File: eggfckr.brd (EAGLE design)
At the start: 91.1 x 31.7 mm, 7 parts, among them U1 ATTINY85-20PU

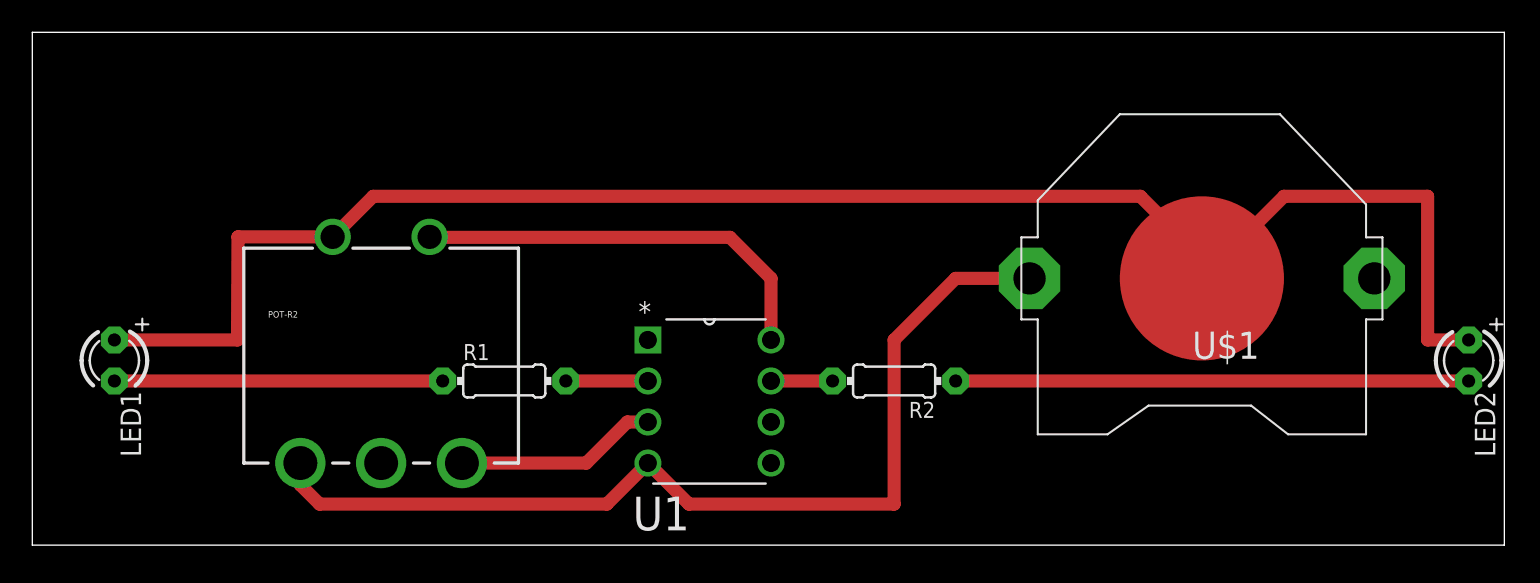
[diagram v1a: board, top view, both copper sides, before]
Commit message: failed linear to log pot convertion
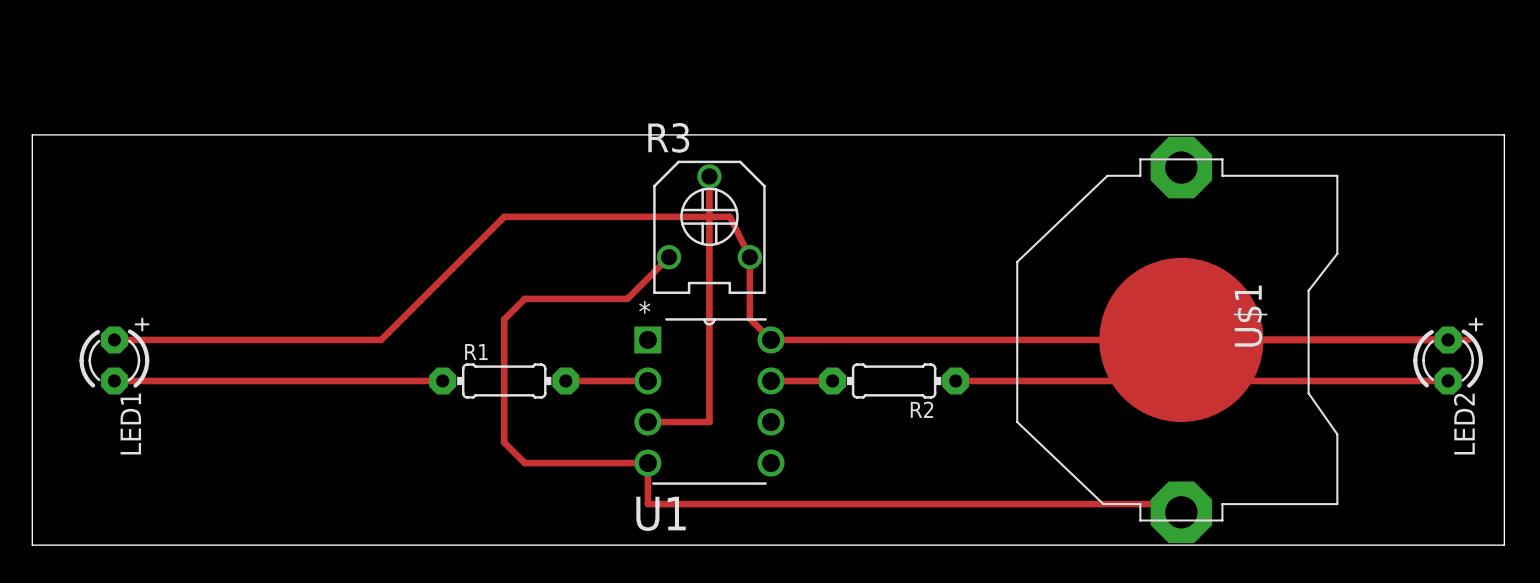
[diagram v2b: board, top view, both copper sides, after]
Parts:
- removed POT-R2: 5K, SparkFun-Electromechanical:POT_PTH
- added R3: (no value), dp_devices:TRIMMER_3306F
- moved U$1 4.02 mm to (71.1, 12.7), turned to 270 degrees
- moved LED2 1.27 mm to (87.6, 11.4)
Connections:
- removed net N$3: POT-R2.S2, U1.8
- net GND: now also R3.1; no longer POT-R2.E@1
- net N$2: now also R3.2; no longer POT-R2.E@2
- net VCC: now also R3.3, U1.8; no longer POT-R2.S1
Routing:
- net N$3: track 26.0 -> 0.00 mm
- net N$2: track 12.6 -> 19.0 mm
- net GND: track 60.8 -> 64.6 mm
- net VCC: track 108.1 -> 109.4 mm
- net N$7: track 31.8 -> 30.5 mm
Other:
- board size 91.1 x 31.7 mm -> 91.1 x 25.4 mm
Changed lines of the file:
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@@
 <plain>
 <wire x1="0" y1="0" x2="91.11" y2="0" width="0" layer="20"/>
-<wire x1="91.11" y1="0" x2="91.11" y2="31.74" width="0" layer="20"/>
-<wire x1="91.11" y1="31.74" x2="0" y2="31.74" width="0" layer="20"/>
-<wire x1="0" y1="31.74" x2="0" y2="0" width="0" layer="20"/>
+<wire x1="91.11" y1="0" x2="91.11" y2="25.39" width="0" layer="20"/>
+<wire x1="91.11" y1="25.39" x2="0" y2="25.39" width="0" layer="20"/>
+<wire x1="0" y1="25.39" x2="0" y2="0" width="0" layer="20"/>
 </plain>
 <attributes>
@@
 </autorouter>
 <elements>
-<element name="POT-R2" library="SparkFun-Electromechanical" package="POT_PTH" value="5K" x="21.59" y="5.08"/>
 <element name="LED1" library="adafruit" package="LED3MM" value="" x="5.08" y="11.43" rot="R270"/>
 <element name="R2" library="adafruit" package="0204/7" value="" x="53.34" y="10.16" rot="R180"/>
@@
 </element>
 <element name="R1" library="adafruit" package="0204/7" value="" x="29.21" y="10.16"/>
-<element name="LED2" library="adafruit" package="LED3MM" value="" x="88.9" y="11.43" rot="R270"/>
-<element name="U$1" library="adafruit" package="CR2032-THRU" value="" x="72.39" y="16.51" rot="R180"/>
+<element name="LED2" library="adafruit" package="LED3MM" value="" x="87.63" y="11.43" rot="R270"/>
+<element name="U$1" library="adafruit" package="CR2032-THRU" value="" x="71.12" y="12.7" rot="R270"/>
+<element name="R3" library="dp_devices" package="TRIMMER_3306F" value="" x="41.91" y="20.32"/>
 </elements>
 <signals>
@@
 <contactref element="U1" pad="7"/>
 <contactref element="R2" pad="2"/>
-<wire x1="45.72" y1="10.16" x2="49.53" y2="10.16" width="0.8128" layer="1"/>
+<wire x1="49.53" y1="10.16" x2="45.72" y2="10.16" width="0.4064" layer="1"/>
 </signal>
 <signal name="N$6">
 <contactref element="R1" pad="1"/>
 <contactref element="LED1" pad="K"/>
-<wire x1="5.08" y1="10.16" x2="25.4" y2="10.16" width="0.8128" layer="1"/>
+<wire x1="25.4" y1="10.16" x2="5.08" y2="10.16" width="0.4064" layer="1"/>
 </signal>
 <signal name="N$7">
 <contactref element="R2" pad="1"/>
 <contactref element="LED2" pad="K"/>
-<wire x1="57.15" y1="10.16" x2="88.9" y2="10.16" width="0.8128" layer="1"/>
+<wire x1="87.63" y1="10.16" x2="57.15" y2="10.16" width="0.4064" layer="1"/>
 </signal>
 <signal name="GND">
 <contactref element="U1" pad="4"/>
-<contactref element="POT-R2" pad="E@1"/>
 <contactref element="U$1" pad="+2"/>
-<wire x1="16.59" y1="5.08" x2="16.59" y2="3.73" width="0.8128" layer="1"/>
-<wire x1="16.59" y1="3.73" x2="17.78" y2="2.54" width="0.8128" layer="1"/>
-<wire x1="17.78" y1="2.54" x2="35.56" y2="2.54" width="0.8128" layer="1"/>
-<wire x1="35.56" y1="2.54" x2="38.1" y2="5.08" width="0.8128" layer="1"/>
-<wire x1="61.722" y1="16.51" x2="57.15" y2="16.51" width="0.8128" layer="1"/>
-<wire x1="57.15" y1="16.51" x2="53.34" y2="12.7" width="0.8128" layer="1"/>
-<wire x1="53.34" y1="12.7" x2="53.34" y2="2.54" width="0.8128" layer="1"/>
-<wire x1="53.34" y1="2.54" x2="40.64" y2="2.54" width="0.8128" layer="1"/>
-<wire x1="40.64" y1="2.54" x2="38.1" y2="5.08" width="0.8128" layer="1"/>
+<contactref element="R3" pad="1"/>
+<wire x1="38.1" y1="5.08" x2="38.1" y2="2.54" width="0.4064" layer="1"/>
+<wire x1="38.1" y1="2.54" x2="70.612" y2="2.54" width="0.4064" layer="1"/>
+<wire x1="70.612" y1="2.54" x2="71.12" y2="2.032" width="0.4064" layer="1"/>
+<wire x1="38.1" y1="5.08" x2="30.48" y2="5.08" width="0.4064" layer="1"/>
+<wire x1="30.48" y1="5.08" x2="29.21" y2="6.35" width="0.4064" layer="1"/>
+<wire x1="29.21" y1="6.35" x2="29.21" y2="13.97" width="0.4064" layer="1"/>
+<wire x1="29.21" y1="13.97" x2="30.48" y2="15.24" width="0.4064" layer="1"/>
+<wire x1="30.48" y1="15.24" x2="36.83" y2="15.24" width="0.4064" layer="1"/>
+<wire x1="36.83" y1="15.24" x2="39.41" y2="17.82" width="0.4064" layer="1"/>
 </signal>
 <signal name="VCC">
-<contactref element="POT-R2" pad="S1"/>
 <contactref element="LED2" pad="A"/>
 <contactref element="LED1" pad="A"/>
 <contactref element="U$1" pad="-"/>
-<wire x1="88.9" y1="12.7" x2="86.36" y2="12.7" width="0.8128" layer="1"/>
-<wire x1="86.36" y1="12.7" x2="86.36" y2="21.59" width="0.8128" layer="1"/>
-<wire x1="86.36" y1="21.59" x2="77.47" y2="21.59" width="0.8128" layer="1"/>
-<wire x1="77.47" y1="21.59" x2="72.39" y2="16.51" width="0.8128" layer="1"/>
-<wire x1="72.39" y1="16.51" x2="71.12" y2="15.24" width="0.8128" layer="1"/>
-<wire x1="71.12" y1="15.24" x2="71.12" y2="16.51" width="0.8128" layer="1"/>
-<wire x1="72.39" y1="16.51" x2="72.39" y2="17.78" width="0.8128" layer="1"/>
-<wire x1="72.39" y1="17.78" x2="68.58" y2="21.59" width="0.8128" layer="1"/>
-<wire x1="68.58" y1="21.59" x2="21.1" y2="21.59" width="0.8128" layer="1"/>
-<wire x1="21.1" y1="21.59" x2="18.59" y2="19.08" width="0.8128" layer="1"/>
-<wire x1="18.59" y1="19.08" x2="12.73" y2="19.08" width="0.8128" layer="1"/>
-<wire x1="12.73" y1="19.08" x2="12.7" y2="12.7" width="0.8128" layer="1"/>
-<wire x1="12.7" y1="12.7" x2="5.08" y2="12.7" width="0.8128" layer="1"/>
-</signal>
-<signal name="N$3">
 <contactref element="U1" pad="8"/>
-<contactref element="POT-R2" pad="S2"/>
-<wire x1="45.72" y1="12.7" x2="45.72" y2="16.51" width="0.8128" layer="1"/>
-<wire x1="45.72" y1="16.51" x2="43.18" y2="19.05" width="0.8128" layer="1"/>
-<wire x1="43.18" y1="19.05" x2="24.62" y2="19.05" width="0.8128" layer="1"/>
-<wire x1="24.62" y1="19.05" x2="24.59" y2="19.08" width="0.8128" layer="1"/>
-</signal>
-<signal name="N$2">
-<contactref element="U1" pad="3"/>
-<contactref element="POT-R2" pad="E@2"/>
-<wire x1="26.59" y1="5.08" x2="34.29" y2="5.08" width="0.8128" layer="1"/>
-<wire x1="34.29" y1="5.08" x2="36.83" y2="7.62" width="0.8128" layer="1"/>
-<wire x1="36.83" y1="7.62" x2="38.1" y2="7.62" width="0.8128" layer="1"/>
+<contactref element="R3" pad="3"/>
+<wire x1="44.41" y1="17.82" x2="44.41" y2="14.01" width="0.4064" layer="1"/>
+<wire x1="44.41" y1="14.01" x2="45.72" y2="12.7" width="0.4064" layer="1"/>
+<wire x1="45.72" y1="12.7" x2="71.12" y2="12.7" width="0.4064" layer="1"/>
+<wire x1="71.12" y1="12.7" x2="87.63" y2="12.7" width="0.4064" layer="1"/>
+<wire x1="5.08" y1="12.7" x2="21.59" y2="12.7" width="0.4064" layer="1"/>
+<wire x1="21.59" y1="12.7" x2="29.21" y2="20.32" width="0.4064" layer="1"/>
+<wire x1="29.21" y1="20.32" x2="43.18" y2="20.32" width="0.4064" layer="1"/>
+<wire x1="43.18" y1="20.32" x2="44.41" y2="17.82" width="0.4064" layer="1"/>
+<wire x1="71.12" y1="12.7" x2="88.9" y2="12.7" width="0.4064" layer="1"/>
+<wire x1="88.9" y1="12.7" x2="87.63" y2="12.7" width="0" layer="19" extent="1-16"/>
 </signal>
 <signal name="N$4">
 <contactref element="U1" pad="2"/>
 <contactref element="R1" pad="2"/>
-<wire x1="33.02" y1="10.16" x2="38.1" y2="10.16" width="0.8128" layer="1"/>
+<wire x1="33.02" y1="10.16" x2="38.1" y2="10.16" width="0.4064" layer="1"/>
+</signal>
+<signal name="N$2">
+<contactref element="U1" pad="3"/>
+<contactref element="R3" pad="2"/>
+<wire x1="41.91" y1="22.82" x2="41.91" y2="7.62" width="0.4064" layer="1"/>
+<wire x1="41.91" y1="7.62" x2="38.1" y2="7.62" width="0.4064" layer="1"/>
 </signal>
 </signals>

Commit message: silluate circuit
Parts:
- removed U$1: (no value), adafruit:CR2032-THRU
- added GND, VCC: (no value), microbuilder:1X01_ROUND
- moved R2 5.29 mm to (57.9, 12.8), turned to 225 degrees
- moved R1 4.45 mm to (24.8, 10.2)
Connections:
- net GND: now also GND.1; no longer U$1.+2
- net VCC: now also VCC.1; no longer U$1.-
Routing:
- net VCC: track 109.4 -> 98.7 mm
- net N$1: track 3.81 -> 9.50 mm
- net GND: track 64.6 -> 58.9 mm
- net N$4: track 5.08 -> 9.53 mm
- net N$6: track 20.3 -> 15.9 mm
- net N$2: track 19.0 -> 17.0 mm
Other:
- board size 91.1 x 25.4 mm -> 91.1 x 30.5 mm

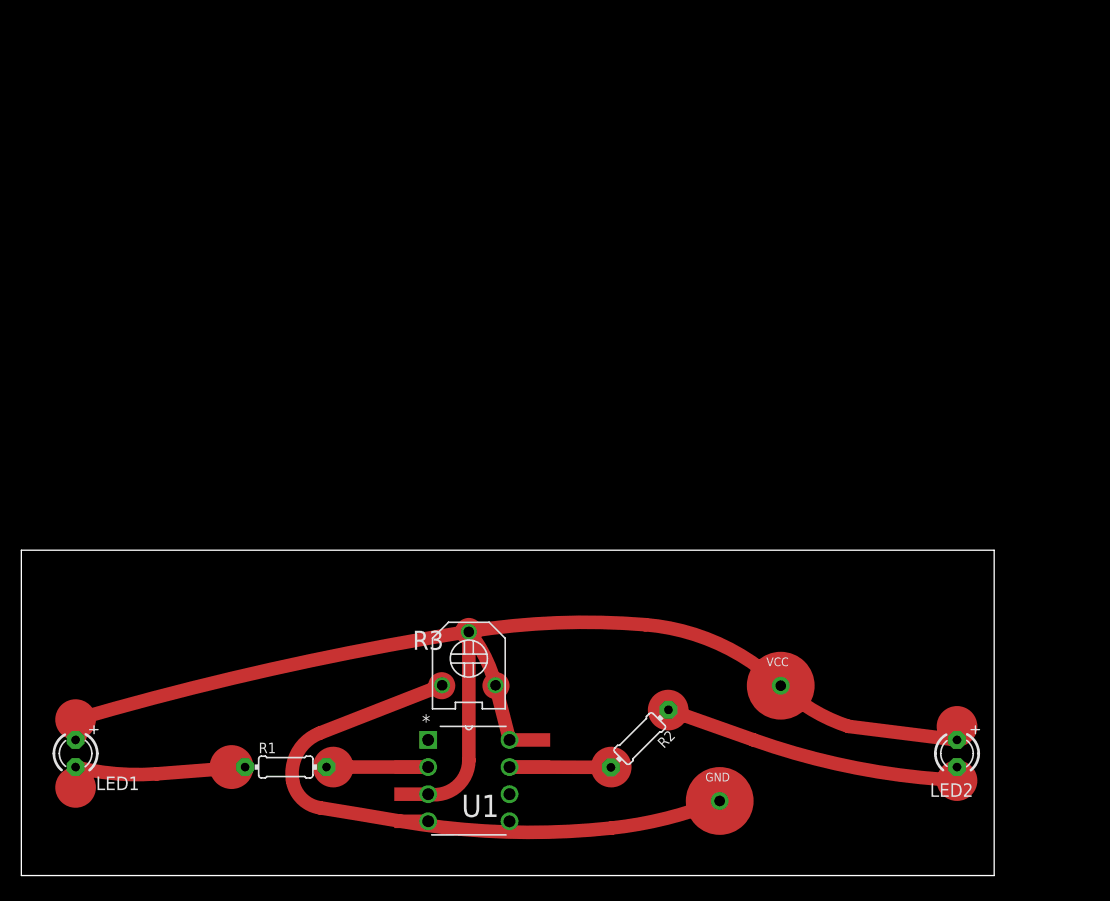
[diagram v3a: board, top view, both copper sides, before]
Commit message: add lib with costum audio jack
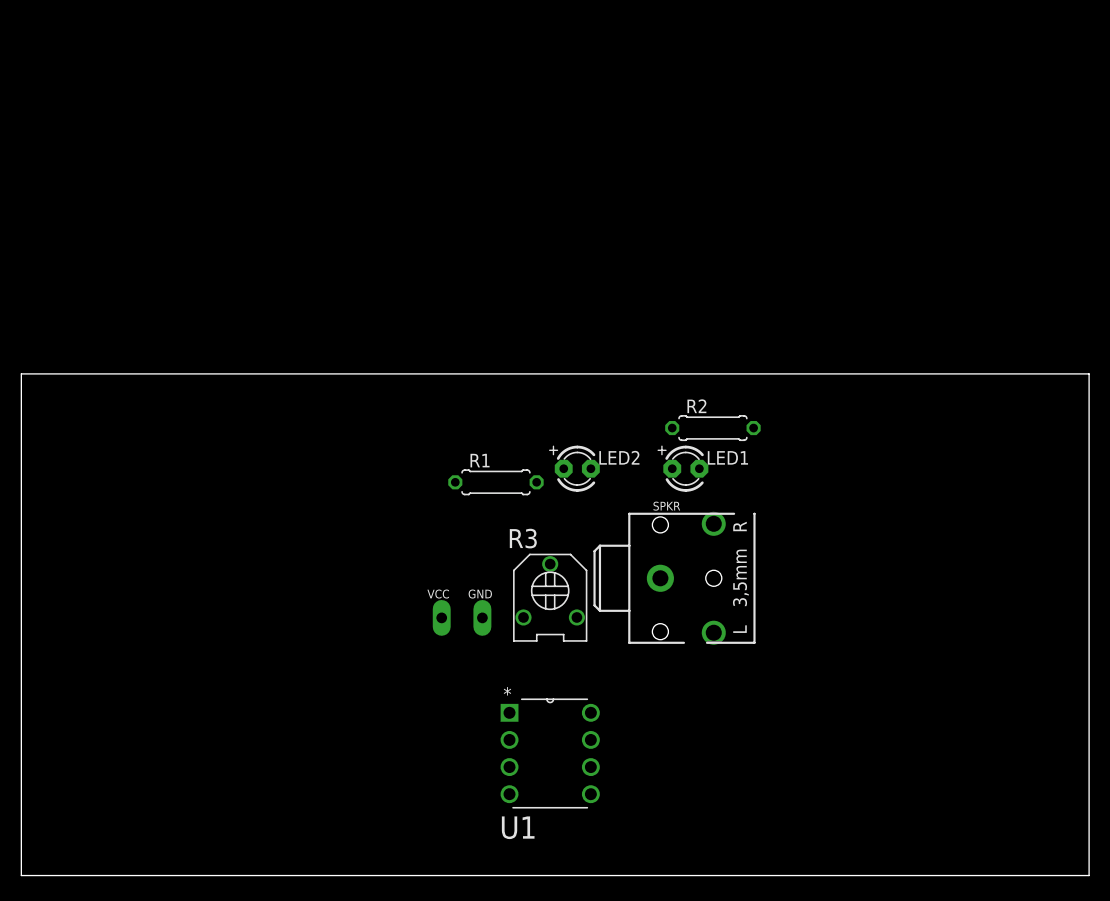
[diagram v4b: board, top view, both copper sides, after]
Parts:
- added SPKR: (no value), eggfckr:STX3100
- GND, VCC: device microbuilder:1X01_ROUND -> eggfckr:1X01_OVAL
- R1, R2: device adafruit:0204/7 -> eggfckr:0207/7
- R3: device dp_devices:TRIMMER_3306F -> eggfckr:TRIMMER_3306F
- U1: device Atmel_By_element14_Batch_1-00:DIP254P762X533-8 -> eggfckr:DIP254P762X533-8
- moved LED1 63.1 mm to (62.2, 38.1), turned to 0 degrees
- moved LED2 44.4 mm to (52.1, 38.1), turned to 0 degrees
- moved R1 33.1 mm to (44.5, 36.8)
- moved VCC 32.4 mm to (39.4, 24.1)
- moved R2 29.9 mm to (64.8, 41.9), turned to 0 degrees
- moved GND 28.1 mm to (43.2, 24.1)
- moved R3 9.92 mm to (49.5, 26.7)
- moved U1 8.03 mm to (53.3, 7.62)
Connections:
- new net LEFT: SPKR.3, U1.6
- new net RIGHT: SPKR.2, U1.5
- net GND: now also SPKR.1
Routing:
- net VCC: track 98.7 -> 0.00 mm
- net GND: track 58.9 -> 0.00 mm
- net N$7: track 30.4 -> 0.00 mm
- net N$2: track 17.0 -> 0.00 mm
- net N$6: track 15.9 -> 0.00 mm
- net N$4: track 9.53 -> 0.00 mm
- net N$1: track 9.50 -> 0.00 mm
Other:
- board size 91.1 x 30.5 mm -> 100 x 47 mm
